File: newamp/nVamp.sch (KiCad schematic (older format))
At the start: 24 parts, among them J1 CONN_01X02, J2 CONN_01X03, J3 CONN_01X02, J4 CONN_01X02, U1 AD8428, U2 ADA4528, U3 ADA4528, U4 AD8428

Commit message: Update amplifier
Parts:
- added C10, C11: CP, Capacitors_THT:CP_Radial_D8.0mm_P3.50mm, symbol CP
- R6, R7: value 33k -> 100k
- gave numbers to parts that had none: 6
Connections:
- net GND: now also C10.2, C11.1
- net VDD: now also C10.1
- net VEE: now also C11.2
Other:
- moved on the sheet: C1, C2, C4, C5, C6, C7, C8, C9, J2

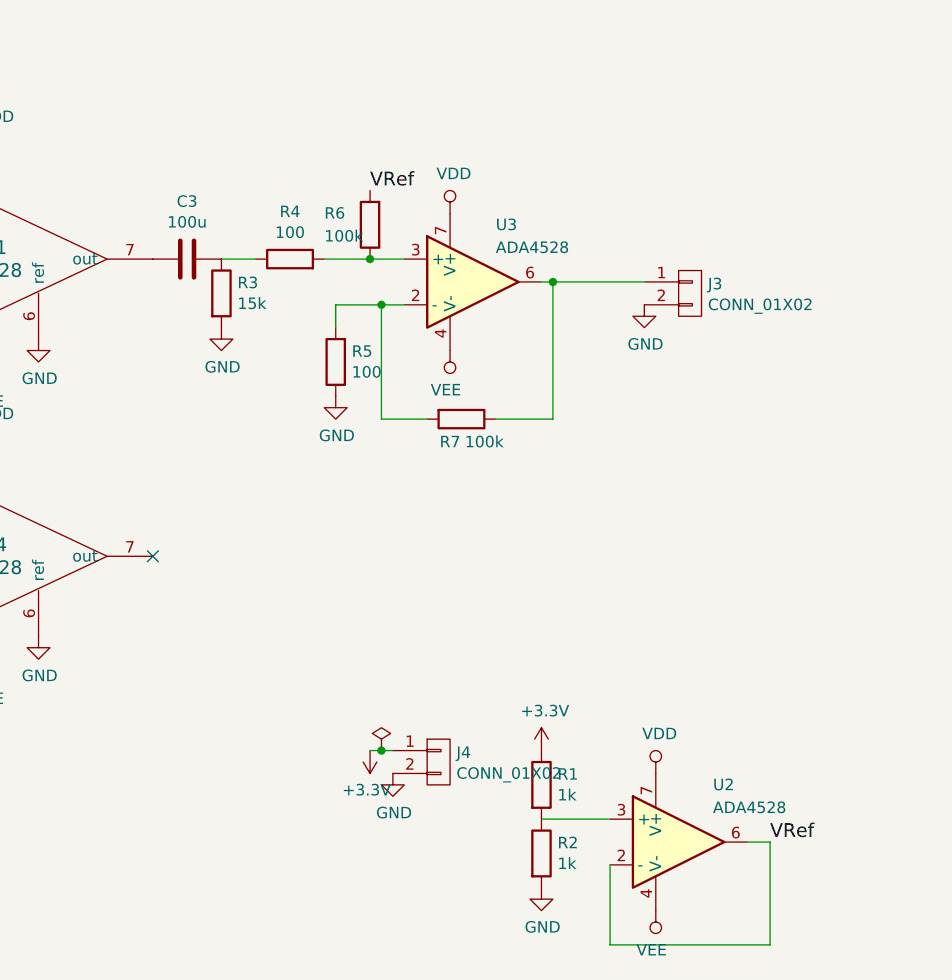
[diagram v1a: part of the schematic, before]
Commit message: Update schematics to add filters and AD4528 single supply
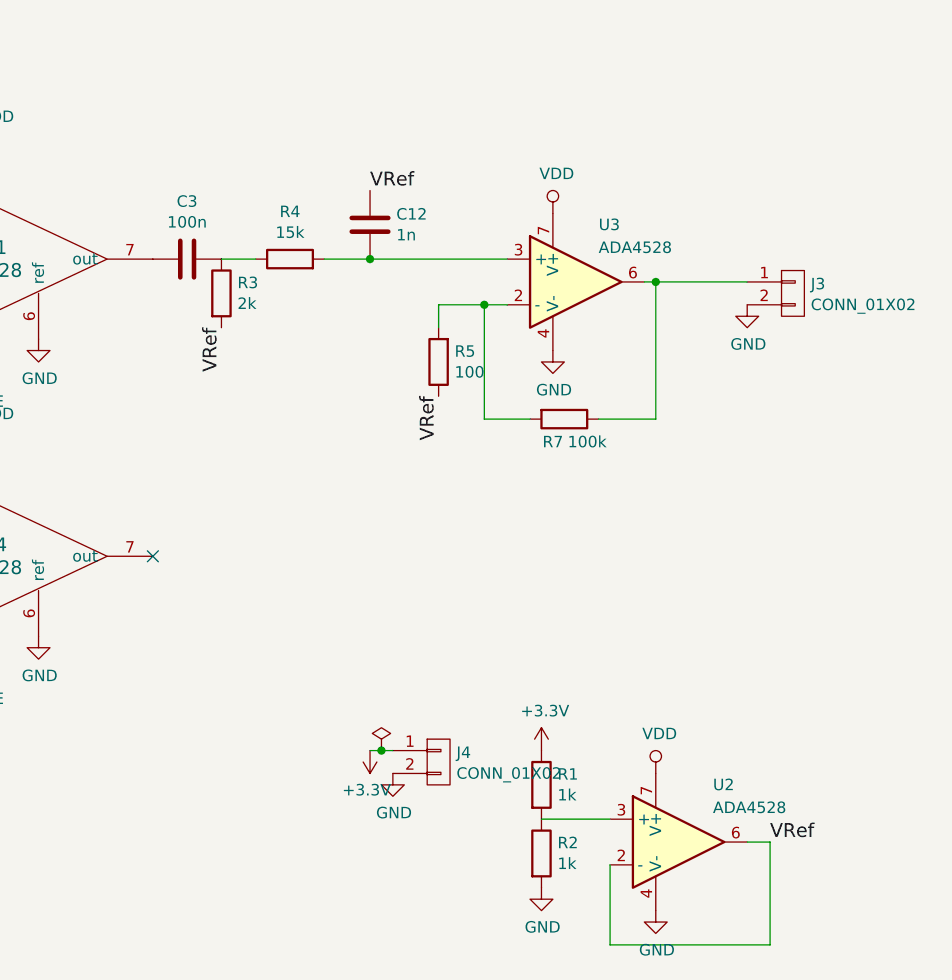
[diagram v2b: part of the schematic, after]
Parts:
- removed R6: 100k, Resistors_SMD:R_0603_HandSoldering, symbol R
- added C12: 1n, symbol C
- C3: value 100u -> 100n
- R3: value 15k -> 2k
- R4: value 100 -> 15k
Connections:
- net GND: now also U2.4 (V-), U3.4 (V-); no longer R3.2, R5.1
- net VEE: no longer U2.4 (V-), U3.4 (V-)
- net VRef: now also R3.2, R5.1, C12.1
- net at R4.2, U3.3 (+): now also C12.2
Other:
- moved on the sheet: J3, R5, R7, U3

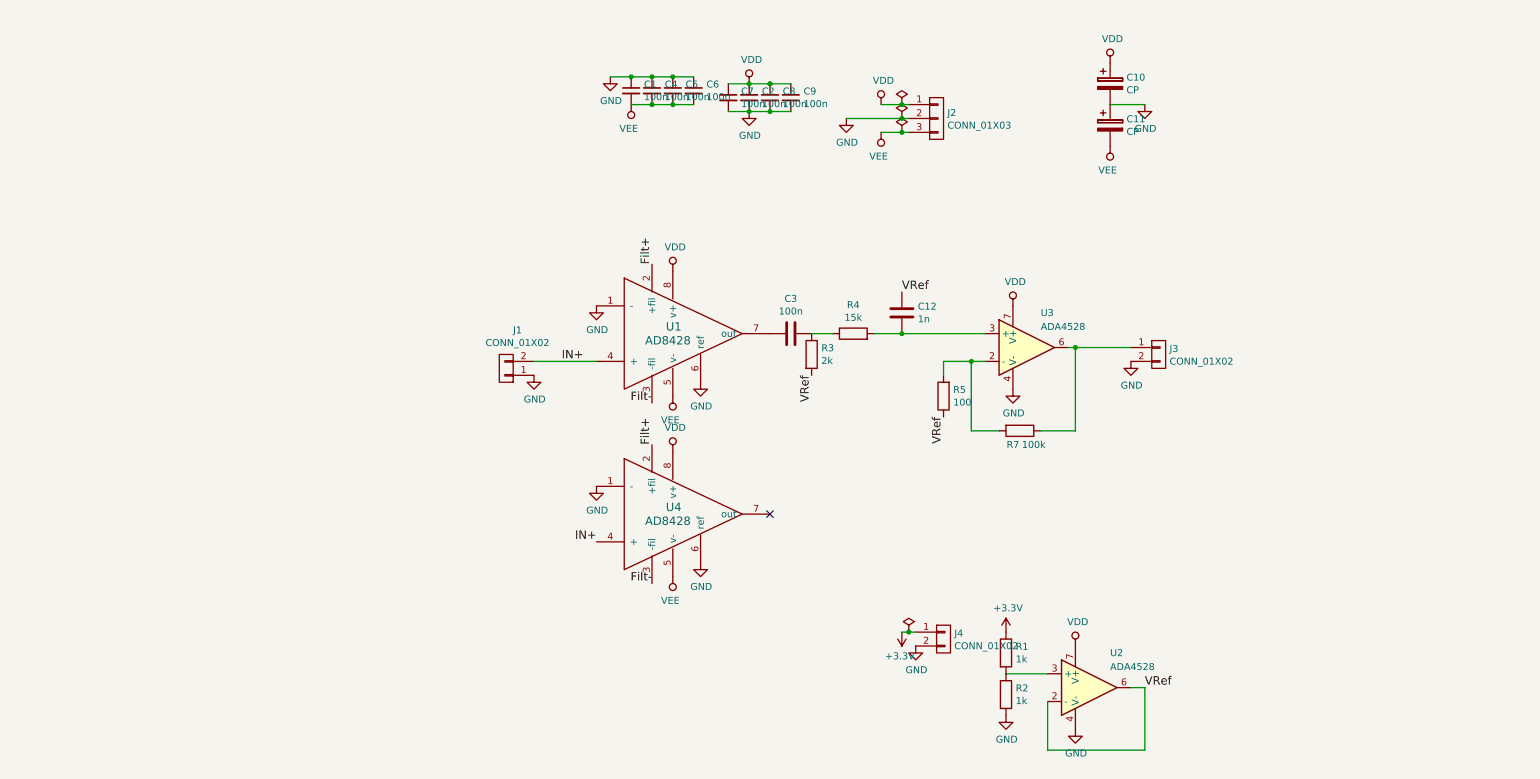
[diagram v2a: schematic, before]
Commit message: Begin working on v2 pcb
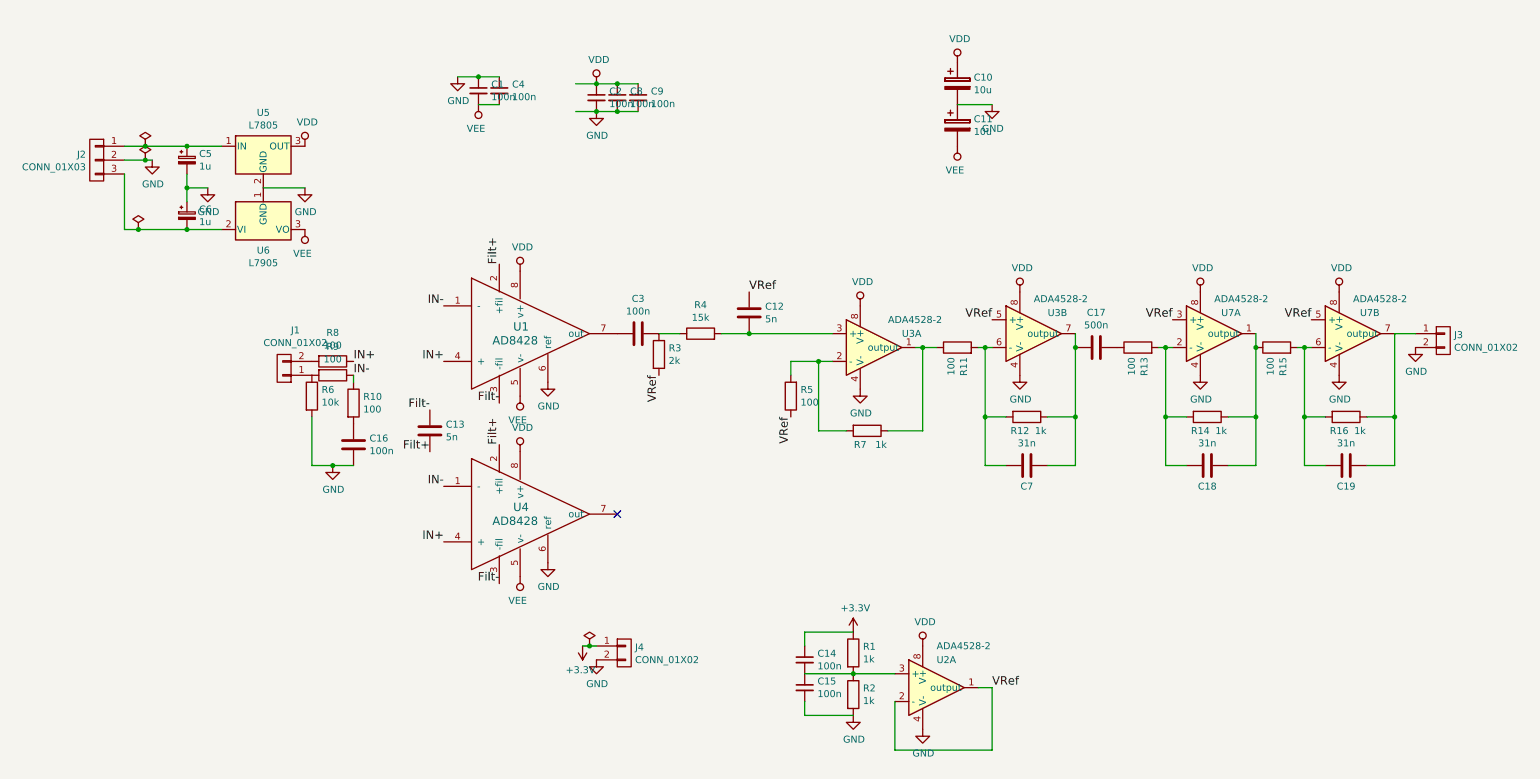
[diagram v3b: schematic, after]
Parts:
- removed C5, C6, C7: 100n, Capacitors_SMD:C_0603_HandSoldering, symbol C_Small
- removed U2, U3: ADA4528, Housings_SSOP:TSSOP-8_3x3mm_Pitch0.65mm, symbol ADA4528
- added C13: 5n, Capacitors_SMD:C_0603_HandSoldering, symbol C
- added C14, C15: 100n, Capacitors_SMD:C_0603_HandSoldering, symbol C_Small
- added C16: 100n, Capacitors_SMD:C_0603_HandSoldering, symbol C
- added C17: 500n, Capacitors_SMD:C_0603_HandSoldering, symbol C
- added C18, C19, C7: 31n, Capacitors_SMD:C_0603_HandSoldering, symbol C
- added C5, C6: 1u, Capacitors_THT:CP_Radial_D5.0mm_P2.50mm, symbol CP_Small
- added R10, R11, R13, R15, R8, R9: 100, Resistors_SMD:R_0603_HandSoldering, symbol R
- added R12, R14, R16: 1k, Resistors_SMD:R_0603_HandSoldering, symbol R
- added R6: 10k, Resistors_SMD:R_0603_HandSoldering, symbol R
- added U2, U3, U7: ADA4528-2, Housings_SSOP:MSOP-8_3x3mm_Pitch0.65mm, symbol ADA4528-2
- added U5: L7805, TO_SOT_Packages_SMD:SOT-23, symbol L7805
- added U6: L7905, TO_SOT_Packages_SMD:SOT-89-3, symbol L7905
- C10, C11: value CP -> 10u; footprint Capacitors_THT:CP_Radial_D8.0mm_P3.50mm -> Capacitors_THT:CP_Radial_D5.0mm_P2.50mm
- C12: value 1n -> 5n; footprint (none) -> Capacitors_SMD:C_0603_HandSoldering
- C3: footprint Capacitors_SMD:C_1210_HandSoldering -> Capacitors_SMD:C_0603_HandSoldering
- R7: value 100k -> 1k
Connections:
- net labels added: IN-
- wire segments 24 -> 56
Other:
- moved on the sheet: C1, C10, C11, C12, C2, C3, C4, C8, C9, J1, J2, J3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

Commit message: Finished version 2.0 of the amplifier PCB
Add better filtering from Ben,
Add differential input
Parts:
- added C20: 62n, Capacitors_SMD:C_0603_HandSoldering, symbol Device:C
- added C22: 620n, Capacitors_SMD:C_0603_HandSoldering, symbol Device:C
- C1, C14, C15, C2, C4, C8, C9: symbol C_Small -> Device:C_Small
- C10, C11: symbol CP -> Device:CP
- C12, C13, C16, C17, C19, C3: symbol C -> Device:C
- C18, C7: value 31n -> 62n; symbol C -> Device:C
- C5, C6: symbol CP_Small -> Device:CP_Small
- J1, J3, J4: symbol CONN_01X02 -> nVamp-rescue:CONN_01X02
- J2: symbol CONN_01X03 -> nVamp-rescue:CONN_01X03
- R1, R10, R11, R13, R15, R2, R3, R4, R5, R6, R7, R8, R9: symbol R -> Device:R
- R12, R14: value 1k -> 1.2k; symbol R -> Device:R
- R16: value 1k -> 2k; symbol R -> Device:R
- U1, U4: symbol AD8428 -> nVamp-rescue:AD8428
- U2, U3, U7: symbol ADA4528-2 -> nVamp-rescue:ADA4528-2
- U5: symbol L7805 -> nVamp-rescue:L7805
- U6: symbol L7905 -> nVamp-rescue:L7905
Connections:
- net labels added: intermediate
- wire segments 56 -> 91
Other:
- moved on the sheet: C10, C11, C17, C18, C19, C7, J3, R12, R13, R14, R15, R16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

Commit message: Lots of changes
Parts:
- removed C16: 100n, Capacitors_SMD:C_0603_HandSoldering, symbol Device:C
- removed R10: 100, Resistors_SMD:R_0603_HandSoldering, symbol Device:R
- removed R6: 10k, Resistors_SMD:R_0603_HandSoldering, symbol Device:R
- removed U5: L7805, TO_SOT_Packages_SMD:SOT-23, symbol nVamp-rescue:L7805
- added U5: MCP1700-1202E_SOT23, Package_TO_SOT_SMD:SOT-23, symbol Regulator_Linear:MCP1700-1202E_SOT23
- R15: value 100 -> 1k
- U2, U3, U7: symbol nVamp-rescue:ADA4528-2 -> nVamp-rescue:ADA4528-2-nVamp-rescue
- U6: symbol nVamp-rescue:L7905 -> nVamp-rescue:L7905-nVamp-rescue
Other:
- moved on the sheet: C1, C10, C11, C12, C13, C17, C18, C19, C2, C20, C22, C3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
